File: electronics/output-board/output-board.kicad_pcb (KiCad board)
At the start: 4 copper layers, 105.2 x 77.5 mm, 95 parts, among them J1 Conn_01x02_Male, J10 Conn_01x02_Male, J11 Conn_01x02_Male, J12 Conn_01x02_Male, J13 Conn_01x02_Male, J14 Arming switch, J15 Conn_01x02_Male, J16 Conn_01x02_Male, J17 Conn_01x02_Male, J18 Conn_01x02_Male, J19 Extra IO, J2 Conn_01x02_Male, J3 12V In, J4 Conn_01x02, J5 SWD Header, J6 Conn_01x02, J7 Conn_01x02_Male, J8 Conn_01x02_Male, J9 Conn_01x02_Male, SW1 SW_Push_Dual, U1 MAX33012EASA+, U2 LD3985M33R_SOT23, U3 STM32F105VBH6, Y1 25MHz 9pF

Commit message: minor changes to output board
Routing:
- net +3V3: track 131.8 -> 146.2 mm
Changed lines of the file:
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@@
   (segment (start 71.249 74.549) (end 71.109 74.549) (width 0.3) (layer "F.Cu") (net 51))
   (segment (start 71.114 74.549) (end 71.249 74.549) (width 0.3) (layer "F.Cu") (net 51))
+  (segment (start 100.98 66.944) (end 101.092 67.056) (width 0.3) (layer "F.Cu") (net 52))
   (segment (start 91.1078 66.07165) (end 91.505748 66.469598) (width 0.3) (layer "F.Cu") (net 52))
+  (segment (start 101.092 72.644) (end 100.792 72.944) (width 0.3) (layer "F.Cu") (net 52))
   (segment (start 71.744 70.104) (end 68.569 70.104) (width 0.3) (layer "F.Cu") (net 52))
+  (segment (start 101.092 73.914) (end 100.584 74.422) (width 0.3) (layer "F.Cu") (net 52))
+  (segment (start 100.948 68.944) (end 101.092 69.088) (width 0.3) (layer "F.Cu") (net 52))
   (segment (start 89.5078 66.0712) (end 89.503324 66.0712) (width 0.3) (layer "F.Cu") (net 52))
   (segment (start 80.313 70.944) (end 80.899 70.358) (width 0.3) (layer "F.Cu") (net 52))
   (segment (start 68.569 70.104) (end 59.806499 61.341499) (width 0.3) (layer "F.Cu") (net 52))
-  (segment (start 100.284 66.944) (end 100.284 68.944) (width 0.3) (layer "F.Cu") (net 52))
+  (segment (start 78.2715 74.6365) (end 78.2715 75.944) (width 0.3) (layer "F.Cu") (net 52))
   (segment (start 60.568647 56.144353) (end 61.14661 56.144353) (width 0.3) (layer "F.Cu") (net 52))
+  (segment (start 101.092 67.056) (end 101.092 69.088) (width 0.3) (layer "F.Cu") (net 52))
   (segment (start 79.834 68.944) (end 80.281 68.944) (width 0.3) (layer "F.Cu") (net 52))
+  (segment (start 78.2715 74.108806) (end 78.2715 74.6365) (width 0.3) (layer "F.Cu") (net 52))
+  (segment (start 76.2765 74.6365) (end 78.2715 74.6365) (width 0.3) (layer "F.Cu") (net 52))
+  (segment (start 71.744 70.104) (end 76.2765 74.6365) (width 0.3) (layer "F.Cu") (net 52))
+  (segment (start 79.392 68.944) (end 78.994 69.342) (width 0.3) (layer "F.Cu") (net 52))
+  (segment (start 78.994 73.386306) (end 78.2715 74.108806) (width 0.3) (layer "F.Cu") (net 52))
   (segment (start 98.821 66.944) (end 98.425 66.548) (width 0.3) (layer "F.Cu") (net 52))
   (segment (start 100.284 68.944) (end 98.789 68.944) (width 0.3) (layer "F.Cu") (net 52))
   (segment (start 100.284 66.944) (end 98.821 66.944) (width 0.3) (layer "F.Cu") (net 52))
   (segment (start 87.917627 64.4712) (end 88.303886 64.857459) (width 0.3) (layer "F.Cu") (net 52))
-  (segment (start 100.284 68.944) (end 100.284 70.944) (width 0.3) (layer "F.Cu") (net 52))
+  (segment (start 79.072 70.944) (end 78.994 70.866) (width 0.3) (layer "F.Cu") (net 52))
+  (segment (start 100.284 68.944) (end 100.948 68.944) (width 0.3) (layer "F.Cu") (net 52))
   (segment (start 91.9078 66.0712) (end 91.9078 66.075129) (width 0.3) (layer "F.Cu") (net 52))
   (segment (start 98.789 68.944) (end 98.425 68.58) (width 0.3) (layer "F.Cu") (net 52))
   (segment (start 98.725 72.944) (end 98.425 72.644) (width 0.3) (layer "F.Cu") (net 52))
   (segment (start 87.9078 62.8712) (end 87.910484 62.8712) (width 0.3) (layer "F.Cu") (net 52))
+  (segment (start 100.284 66.944) (end 100.98 66.944) (width 0.3) (layer "F.Cu") (net 52))
+  (segment (start 100.284 70.944) (end 101.014 70.944) (width 0.3) (layer "F.Cu") (net 52))
   (segment (start 100.284 72.944) (end 98.725 72.944) (width 0.3) (layer "F.Cu") (net 52))
+  (segment (start 100.792 72.944) (end 100.284 72.944) (width 0.3) (layer "F.Cu") (net 52))
+  (segment (start 100.584 74.422) (end 99.314 74.422) (width 0.3) (layer "F.Cu") (net 52))
   (segment (start 59.806499 56.906501) (end 60.568647 56.144353) (width 0.3) (layer "F.Cu") (net 52))
+  (segment (start 101.014 70.944) (end 101.092 70.866) (width 0.3) (layer "F.Cu") (net 52))
   (segment (start 59.806499 61.341499) (end 59.806499 56.906501) (width 0.3) (layer "F.Cu") (net 52))
   (segment (start 90.3078 66.0712) (end 90.321191 66.0712) (width 0.3) (layer "F.Cu") (net 52))
   (segment (start 91.9078 66.075129) (end 92.303036 66.470365) (width 0.3) (layer "F.Cu") (net 52))
   (segment (start 100.284 70.944) (end 98.757 70.944) (width 0.3) (layer "F.Cu") (net 52))
-  (segment (start 73.30852 71.66852) (end 79.10948 71.66852) (width 0.3) (layer "F.Cu") (net 52))
   (segment (start 98.757 70.944) (end 98.425 70.612) (width 0.3) (layer "F.Cu") (net 52))
-  (segment (start 79.10948 71.66852) (end 79.834 70.944) (width 0.3) (layer "F.Cu") (net 52))
-  (segment (start 71.744 70.104) (end 73.30852 71.66852) (width 0.3) (layer "F.Cu") (net 52))
+  (segment (start 85.852 71.374) (end 80.01 77.216) (width 0.3) (layer "F.Cu") (net 52))
+  (segment (start 101.092 72.644) (end 101.092 73.914) (width 0.3) (layer "F.Cu") (net 52))
+  (segment (start 78.994 69.342) (end 78.994 70.866) (width 0.3) (layer "F.Cu") (net 52))
+  (segment (start 80.01 77.216) (end 79.5435 77.216) (width 0.3) (layer "F.Cu") (net 52))
+  (segment (start 101.092 69.088) (end 101.092 70.866) (width 0.3) (layer "F.Cu") (net 52))
   (segment (start 80.281 68.944) (end 80.899 68.326) (width 0.3) (layer "F.Cu") (net 52))
-  (segment (start 78.2715 75.944) (end 79.10948 75.10602) (width 0.3) (layer "F.Cu") (net 52))
+  (segment (start 96.266 71.374) (end 85.852 71.374) (width 0.3) (layer "F.Cu") (net 52))
+  (segment (start 79.834 68.944) (end 79.392 68.944) (width 0.3) (layer "F.Cu") (net 52))
   (segment (start 90.321191 66.0712) (end 90.715667 66.465676) (width 0.3) (layer "F.Cu") (net 52))
-  (segment (start 100.284 70.944) (end 100.284 72.944) (width 0.3) (layer "F.Cu") (net 52))
-  (segment (start 79.834 68.944) (end 79.834 70.944) (width 0.3) (layer "F.Cu") (net 52))
   (segment (start 79.834 70.944) (end 80.313 70.944) (width 0.3) (layer "F.Cu") (net 52))
+  (segment (start 78.994 70.866) (end 78.994 73.386306) (width 0.3) (layer "F.Cu") (net 52))
   (segment (start 91.1078 66.0712) (end 91.1078 66.07165) (width 0.3) (layer "F.Cu") (net 52))
+  (segment (start 99.314 74.422) (end 96.266 71.374) (width 0.3) (layer "F.Cu") (net 52))
   (segment (start 87.9078 64.4712) (end 87.917627 64.4712) (width 0.3) (layer "F.Cu") (net 52))
-  (segment (start 79.10948 75.10602) (end 79.10948 71.66852) (width 0.3) (layer "F.Cu") (net 52))
   (segment (start 89.503324 66.0712) (end 89.098511 65.666387) (width 0.3) (layer "F.Cu") (net 52))
+  (segment (start 79.5435 77.216) (end 78.2715 75.944) (width 0.3) (layer "F.Cu") (net 52))
+  (segment (start 101.092 70.866) (end 101.092 72.644) (width 0.3) (layer "F.Cu") (net 52))
   (segment (start 87.910484 62.8712) (end 88.311746 63.272462) (width 0.3) (layer "F.Cu") (net 52))
+  (segment (start 79.834 70.944) (end 79.072 70.944) (width 0.3) (layer "F.Cu") (net 52))
   (via (at 90.715667 66.465676) (size 0.4) (drill 0.2) (layers "F.Cu" "B.Cu") (net 52))
   (via (at 91.505748 66.469598) (size 0.4) (drill 0.2) (layers "F.Cu" "B.Cu") (net 52))
@@
   (segment (start 92.380671 66.548) (end 92.303036 66.470365) (width 0.3) (layer "In2.Cu") (net 52))
   (segment (start 97.917 67.818) (end 98.425 68.326) (width 0.3) (layer "In2.Cu") (net 52))
-  (segment (start 81.026 70.231) (end 89.661294 70.231) (width 0.3) (layer "In2.Cu") (net 52))
   (segment (start 91.505748 66.469598) (end 91.505748 66.486748) (width 0.3) (layer "In2.Cu") (net 52))
   (segment (start 95.885 68.326) (end 92.075 68.326) (width 0.3) (layer "In2.Cu") (net 52))
@@
   (segment (start 98.425 70.612) (end 98.171 70.612) (width 0.3) (layer "In2.Cu") (net 52))
   (segment (start 98.425 68.326) (end 98.425 68.58) (width 0.3) (layer "In2.Cu") (net 52))
-  (segment (start 92.513783 69.781489) (end 95.376294 72.644) (width 0.3) (layer "In2.Cu") (net 52))
   (segment (start 89.098511 65.666387) (end 89.098511 66.335267) (width 0.3) (layer "In2.Cu") (net 52))
   (segment (start 92.904805 69.273489) (end 95.054489 69.273489) (width 0.3) (layer "In2.Cu") (net 52))
-  (segment (start 90.110805 69.781489) (end 92.513783 69.781489) (width 0.3) (layer "In2.Cu") (net 52))
   (segment (start 98.171 70.612) (end 95.885 68.326) (width 0.3) (layer "In2.Cu") (net 52))
   (segment (start 88.311746 63.272462) (end 85.952538 63.272462) (width 0.3) (layer "In2.Cu") (net 52))
@@
   (segment (start 98.425 66.548) (end 92.380671 66.548) (width 0.3) (layer "In2.Cu") (net 52))
   (segment (start 92.837 67.818) (end 97.917 67.818) (width 0.3) (layer "In2.Cu") (net 52))
-  (segment (start 89.661294 70.231) (end 90.110805 69.781489) (width 0.3) (layer "In2.Cu") (net 52))
   (segment (start 95.054489 69.273489) (end 98.425 72.644) (width 0.3) (layer "In2.Cu") (net 52))
-  (segment (start 95.376294 72.644) (end 98.425 72.644) (width 0.3) (layer "In2.Cu") (net 52))
   (segment (start 82.06768 64.07072) (end 81.6732 64.4652) (width 0.3) (layer "F.Cu") (net 56))
   (segment (start 87.1078 64.4712) (end 86.70732 64.07072) (width 0.3) (layer "F.Cu") (net 56))

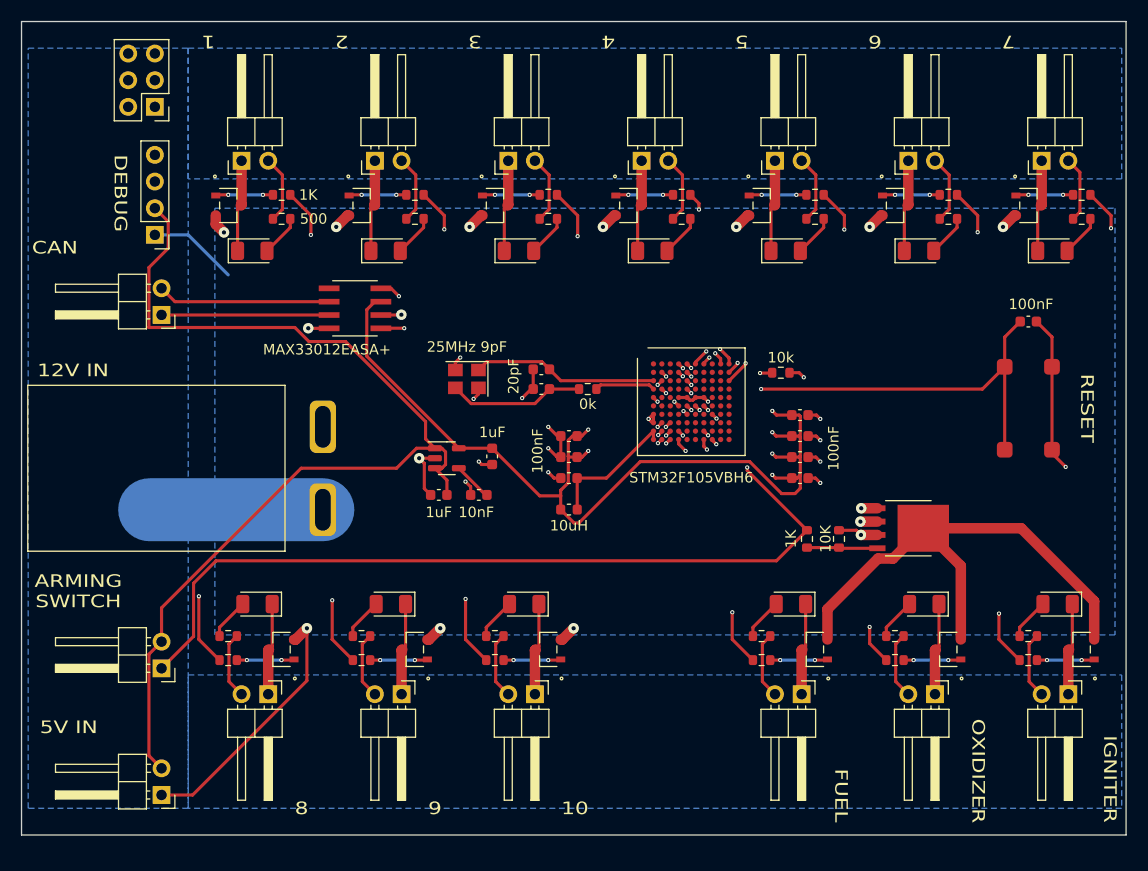
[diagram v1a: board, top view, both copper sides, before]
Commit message: added power leds and ignition detection
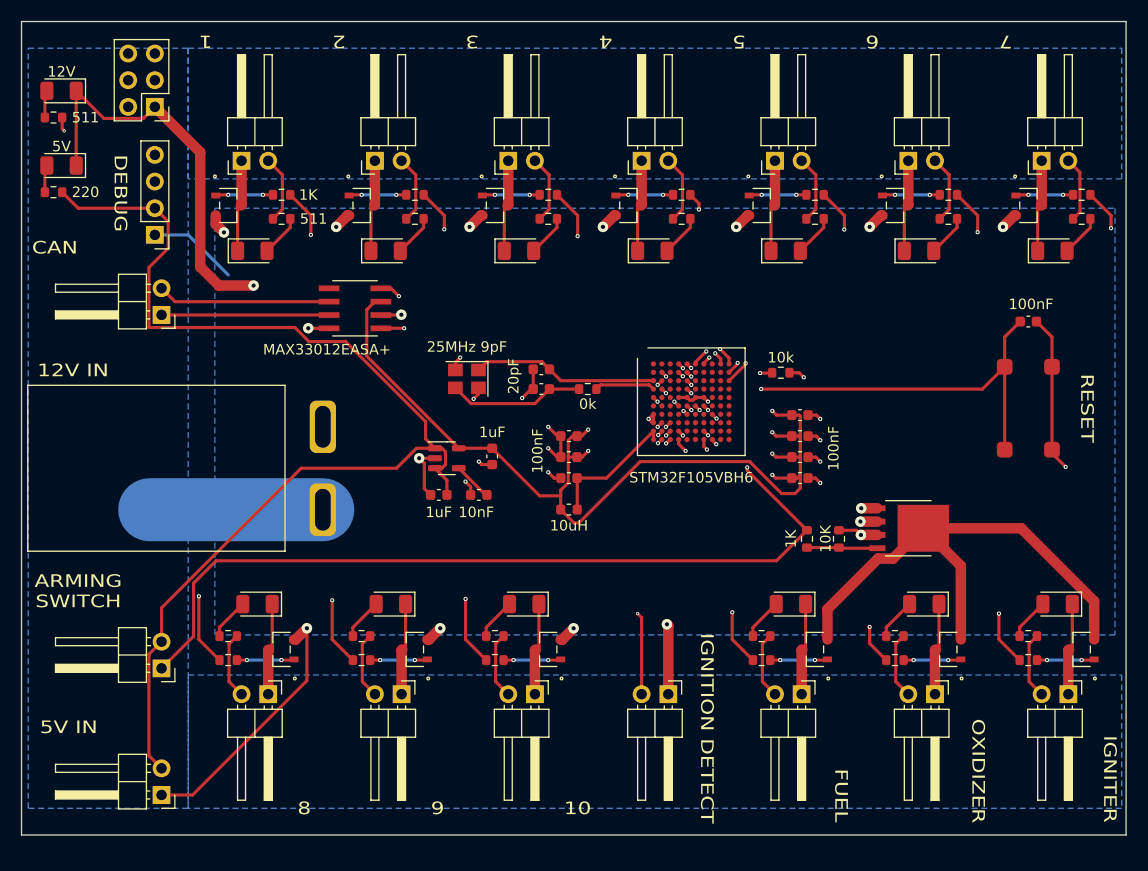
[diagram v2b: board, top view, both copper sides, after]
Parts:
- added D14: 12V, LED_SMD:LED_1206_3216Metric, F.Cu at (30.7, 36.1)
- added D15: 5V, LED_SMD:LED_1206_3216Metric, F.Cu at (30.7, 43.2)
- added J20: Ignition Detector, CustomFootprints:LatchingConnector2POS, F.Cu at (88.5, 93.5)
- added R31: 511, Resistor_SMD:R_0603_1608Metric, F.Cu at (30.0, 38.6)
- added R32: 220, Resistor_SMD:R_0603_1608Metric, F.Cu at (30.0, 45.7)
- R10, R11, R2, R20, R26, R28, R30, R4, R5, R6, R7, R8, R9: value 500 -> 511
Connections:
- J19 pad 1: Net-(J19-Pad1) -> GND
- U3 pad H2: Net-(J19-Pad1) -> Net-(U3-PadH2)
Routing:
- net Net-(J19-Pad1): track 80.7 -> 0.00 mm, vias 1 -> 0
- net GND: track 108.3 -> 154.0 mm, vias 33 -> 35
- net Net-(U3-PadH2): track 0.00 -> 27.0 mm, vias 0 -> 2
- net +5V: track 100.7 -> 110.2 mm
- net Net-(D15-Pad2): track 0.00 -> 2.62 mm
- net Net-(D14-Pad2): track 0.00 -> 2.62 mm
- net +12V: track 99.6 -> 100.9 mm, vias 0 -> 1
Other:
- board text added: "IGNITION DETECT"

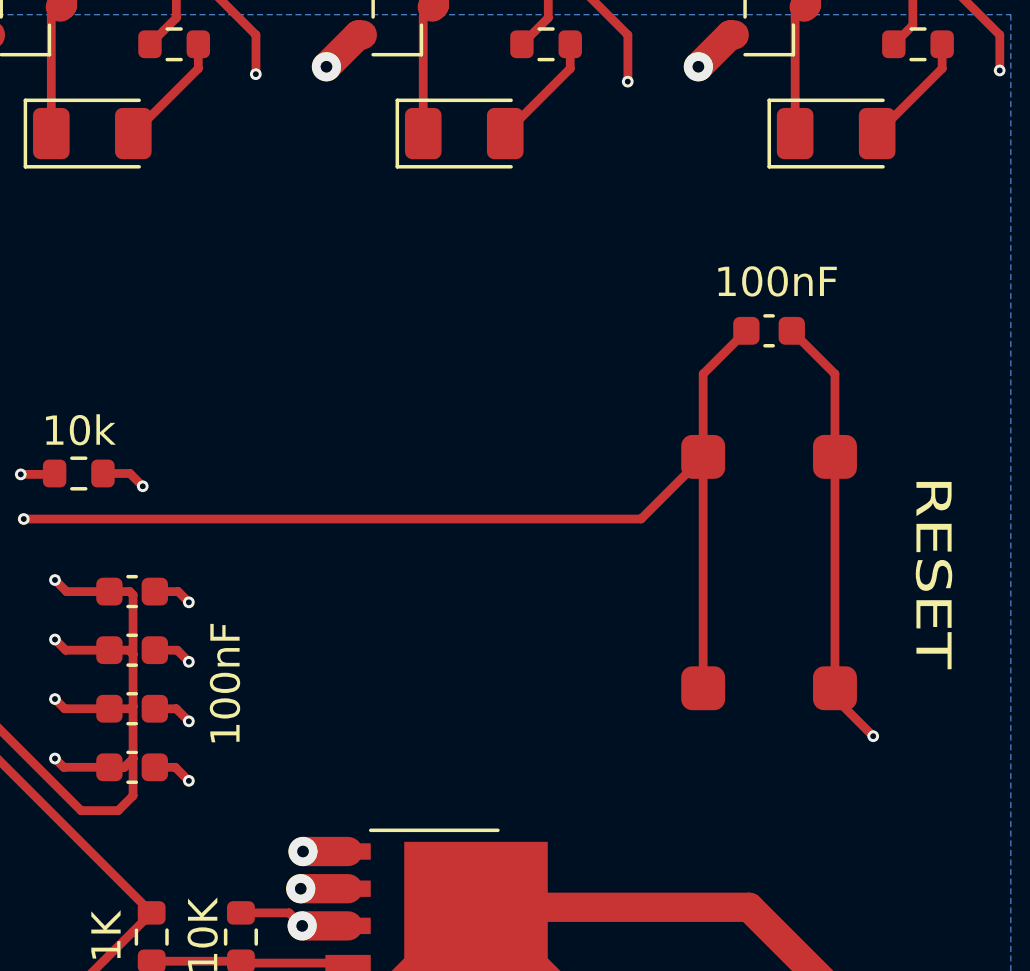
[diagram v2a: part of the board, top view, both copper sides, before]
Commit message: Fix footprint paths and add SEDS logo to output board
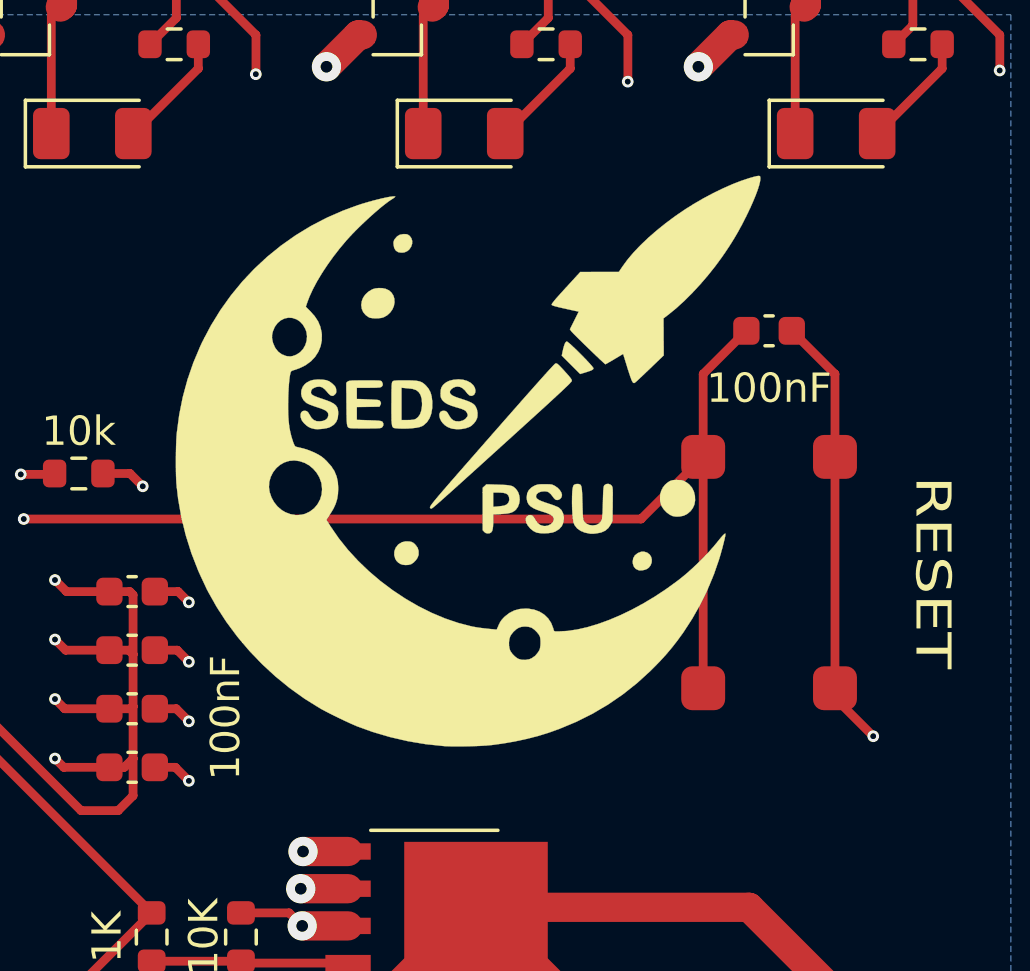
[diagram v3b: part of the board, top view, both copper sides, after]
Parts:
- added Ref**: Val**, CustomFootprints:seds-logo, F.Cu at (112.5, 62.2)
